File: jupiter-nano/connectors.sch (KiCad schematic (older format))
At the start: 0 parts

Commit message: WIP, connectors almost done
- still to do:
  - JTAG signals on PIO pins
  - USB-UART bridge
  - extra PIO on the header pins
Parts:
- added C28: 10uF, symbol Device:C
- added J5: Micro_SD_Card_Det_Hirose_DM3AT, symbol Connector:Micro_SD_Card_Det_Hirose_DM3AT
- added J5, J7, J8: USB_B_Micro, symbol Connector:USB_B_Micro
- added J6: Conn_01x02, symbol Connector_Generic:Conn_01x02
- added J9: Conn_ARM_JTAG_SWD_10, symbol Connector:Conn_ARM_JTAG_SWD_10
- added M3, MH4: MountingHole, symbol Mechanical:MountingHole
- added MH1, MH2: Conn_01x01, symbol Connector_Generic:Conn_01x01
- added R30: 10K, symbol Device:R_Small
- added R31: 68k, symbol Device:R_Small
- added R32, R33, R34: 68K, symbol Device:R_Small
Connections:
- new net CGND: J5.11 (SHIELD), J5.6 (Shield), J7.6 (Shield), J8.6 (Shield), MH1.1 (Pin_1), MH2.1 (Pin_1)
- new net GND: C28.1, J5.5 (GND), J5.6 (VSS), J7.5 (GND), J8.5 (GND), J9.3 (GND), J9.5 (GND), J9.9 (GNDDetect)
- new net HSIC_DATA: J6.2 (Pin_2)
- new net HSIC_STROBE: J6.1 (Pin_1)
- new net JTAG_TCK_PD14: J9.4 (SWDCLK/TCK)
- new net JTAG_TDI_PD15: J9.8 (NC/TDI)
- new net JTAG_TDO_PD16: J9.6 (SWO/TDO)
- new net JTAG_TMS_PD17: J9.2 (SWDIO/TMS)
- new net NRST: J9.10 (~RESET~)
- new net SDMMC1_CK: J5.5 (CLK)
- new net SDMMC1_CMD: J5.3 (CMD), R30.1
- new net SDMMC1_DAT0: J5.7 (DAT0), R33.1
- new net SDMMC1_DAT1: J5.8 (DAT1), R34.1
- new net SDMMC1_DAT2: J5.1 (DAT2), R31.1
- new net SDMMC1_DAT3: J5.2 (DAT3/CD), R32.1
- new net USBA_M: J5.2 (D-)
- new net USBA_P: J5.3 (D+)
- new net USBB_M: J7.2 (D-)
- new net USBB_P: J7.3 (D+)
- new net USBU_M: J8.2 (D-)
- new net USBU_P: J8.3 (D+)
- new net VBUS: J5.1 (VBUS), J7.1 (VBUS), J8.1 (VBUS)
- new net VDD_3V3: C28.2, J5.4 (VDD), J9.1 (VTref), R30.2, R31.2, R32.2, R33.2, R34.2
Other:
- note added: "JTAG"
- note added: "MicroSD"
- note added: "Mounting Holes"
- note added: "TODO: JTAG"
- note added: "TODO: card detect"
- note added: "USB"
- note added: "USB-UART Bridge"

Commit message: WIP, USB-UART and JTAG done
- minor clean up and SD Card form factor still left
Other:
- note removed: "TODO: JTAG"
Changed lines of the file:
@@
 Text Notes 6750 2650 0    79   ~ 0
 TODO: card detect
-Text Notes 3700 2200 0    79   ~ 0
-TODO: JTAG
 $Comp
 L starcat:CGND #PWR?

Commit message: cleanup
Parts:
- added R120: 10K, symbol Device:R_Small
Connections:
- net GND: now also R120.1
- net VDD_3V3: now also J5.10 (DET_A)
- net SDMMC1_CARD_DET: now reaches J5.9 (DET_B)
- net SDMMC1_CARD_DET: now also R120.2
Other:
- note added: "Native HSIC"
- note added: "Native USB Device"
- note added: "Native USB Host"
- note removed: "TODO: card detect"
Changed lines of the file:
@@
 Wire Wire Line
 	8500 2450 9550 2450
-Text Notes 6750 2650 0    79   ~ 0
-TODO: card detect
 $Comp
 L starcat:CGND #PWR?
@@
 Wire Wire Line
 	3100 2300 3100 2350
+Text Notes 1150 3850 0    79   ~ 0
+Native USB Host
+Text Notes 4200 3850 0    79   ~ 0
+Native USB Device
+Text Notes 7000 3800 0    79   ~ 0
+Native HSIC
+Wire Wire Line
+	6650 2650 6900 2650
+Wire Wire Line
+	6900 2650 6900 2900
+$Comp
+L Device:R_Small R120
+U 1 1 601FABB8
+P 6900 3000
+F 0 "R120" H 6841 2954 50  0000 R CNN
+F 1 "10K" H 6841 3045 50  0000 R CNN
+F 2 "" H 6900 3000 50  0001 C CNN
+F 3 "~" H 6900 3000 50  0001 C CNN
+	1    6900 3000
+	-1   0    0    1
+$EndComp
+Wire Wire Line
+	6900 3100 6900 3200
+$Comp
+L power:GND #PWR?
+U 1 1 602008BF
+P 6900 3200
+F 0 "#PWR?" H 6900 2950 50  0001 C CNN
+F 1 "GND" H 6905 3027 50  0000 C CNN
+F 2 "" H 6900 3200 50  0001 C CNN
+F 3 "" H 6900 3200 50  0001 C CNN
+	1    6900 3200
+	1    0    0    -1
+$EndComp
+Wire Wire Line
+	6900 2650 9550 2650
+Connection ~ 6900 2650
+Text GLabel 9550 2650 2    50   Input ~ 0
+SDMMC1_CARD_DET
+Wire Wire Line
+	6650 2550 9550 2550
+Text GLabel 9550 2550 2    50   Input ~ 0
+VDD_3V3
 $EndSCHEMATC

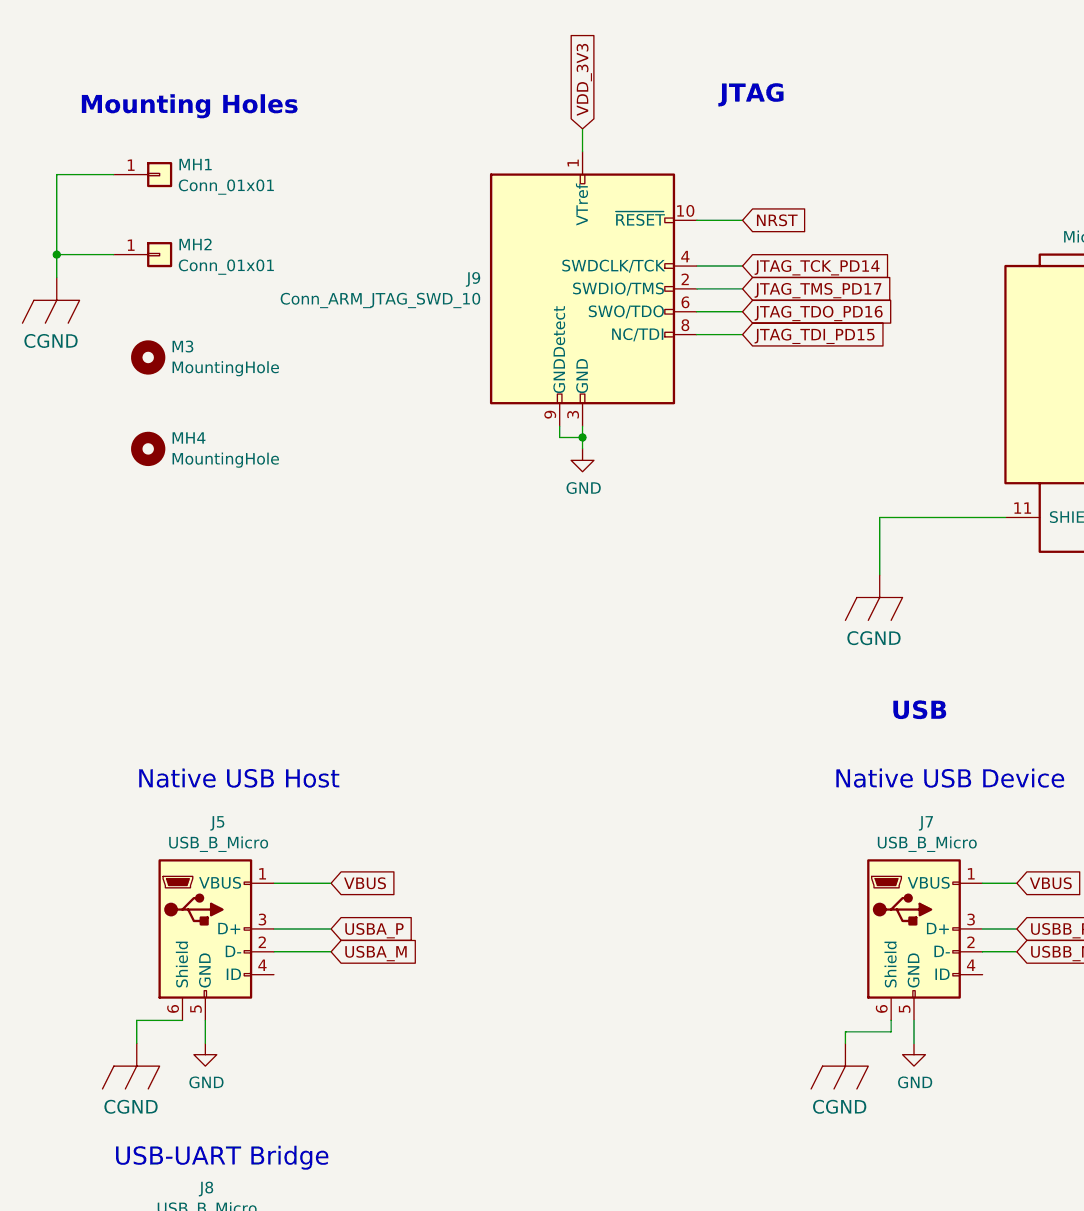
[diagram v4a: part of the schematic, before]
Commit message: add USBA VBUS sense; remove mounting holes
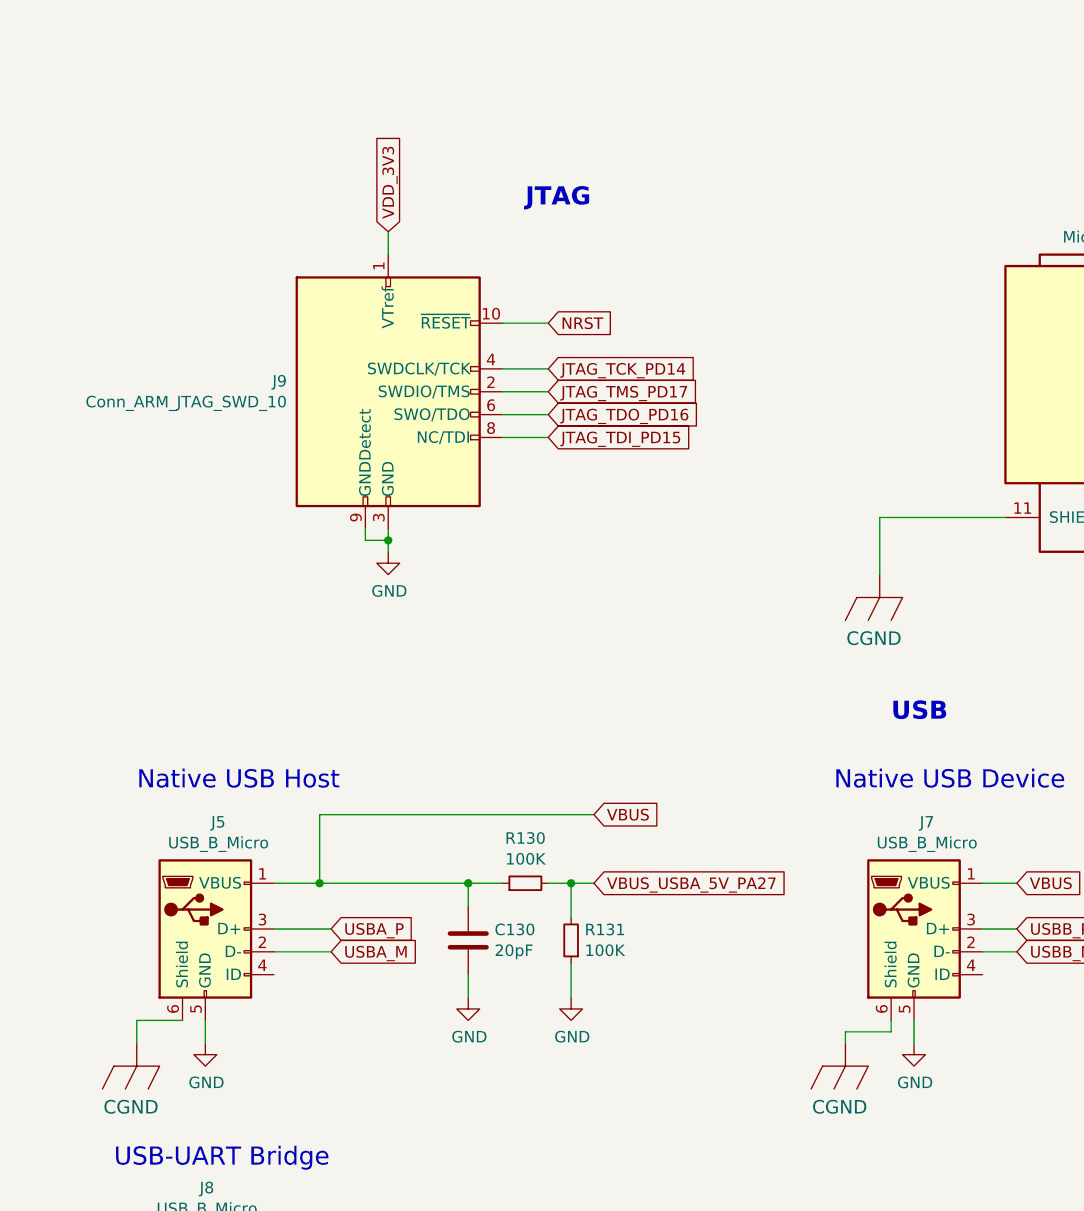
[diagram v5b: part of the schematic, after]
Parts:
- removed M3, MH4: MountingHole, symbol Mechanical:MountingHole
- removed MH1, MH2: Conn_01x01, symbol Connector_Generic:Conn_01x01
- added C130: 20pF, symbol Device:C
- added R130, R131: 100K, symbol Device:R_Small
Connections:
- net GND: now also C130.2, R131.1
- net VBUS: now also C130.1, R130.1
- new net VBUS_USBA_5V_PA27: R130.2, R131.2
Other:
- note removed: "Mounting Holes"
- moved on the sheet: J9
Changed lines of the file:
@@
 Comment4 ""
 $EndDescr
-Text Notes 900  900  0    79   ~ 16
-Mounting Holes
-$Comp
-L Connector_Generic:Conn_01x01 MH1
-U 1 1 600DDBE3
-P 1250 1150
-F 0 "MH1" H 1330 1192 50  0000 L CNN
-F 1 "Conn_01x01" H 1330 1101 50  0000 L CNN
-F 2 "" H 1250 1150 50  0001 C CNN
-F 3 "~" H 1250 1150 50  0001 C CNN
-	1    1250 1150
-	1    0    0    -1
-$EndComp
-$Comp
-L Connector_Generic:Conn_01x01 MH2
-U 1 1 600DE109
-P 1250 1500
-F 0 "MH2" H 1330 1542 50  0000 L CNN
-F 1 "Conn_01x01" H 1330 1451 50  0000 L CNN
-F 2 "" H 1250 1500 50  0001 C CNN
-F 3 "~" H 1250 1500 50  0001 C CNN
-	1    1250 1500
-	1    0    0    -1
-$EndComp
-$Comp
-L Mechanical:MountingHole M3
-U 1 1 600DE96A
-P 1200 1950
-F 0 "M3" H 1300 1996 50  0000 L CNN
-F 1 "MountingHole" H 1300 1905 50  0000 L CNN
-F 2 "" H 1200 1950 50  0001 C CNN
-F 3 "~" H 1200 1950 50  0001 C CNN
-	1    1200 1950
-	1    0    0    -1
-$EndComp
-$Comp
-L Mechanical:MountingHole MH4
-U 1 1 600DEB93
-P 1200 2350
-F 0 "MH4" H 1300 2396 50  0000 L CNN
-F 1 "MountingHole" H 1300 2305 50  0000 L CNN
-F 2 "" H 1200 2350 50  0001 C CNN
-F 3 "~" H 1200 2350 50  0001 C CNN
-	1    1200 2350
-	1    0    0    -1
-$EndComp
-Wire Wire Line
-	1050 1150 800  1150
-Wire Wire Line
-	800  1150 800  1500
-Wire Wire Line
-	800  1500 1050 1500
-Wire Wire Line
-	800  1500 800  1600
-Connection ~ 800  1500
-Text Notes 3700 850  0    79   ~ 16
+Text Notes 2850 1300 0    79   ~ 16
 JTAG
 Text Notes 7450 800  0    79   ~ 16
@@
 	1750 4550 2000 4550
 Wire Wire Line
-	1750 4250 2000 4250
-Wire Wire Line
 	1450 4850 1450 4950
 Wire Wire Line
@@
 Wire Wire Line
 	1400 6450 1400 6500
-Text GLabel 2000 4250 2    50   Input ~ 0
-VBUS
+Text GLabel 3150 4250 2    50   Input ~ 0
+VBUS_USBA_5V_PA27
 Text GLabel 5000 4250 2    50   Input ~ 0
 VBUS
@@
 Wire Wire Line
 	8500 2450 9550 2450
-$Comp
-L starcat:CGND #PWR?
-U 1 1 6019D543
-P 800 1700
-F 0 "#PWR?" H 800 1800 79  0001 C CNN
-F 1 "CGND" H 775 1520 59  0000 C CNN
-F 2 "" H 800 1800 79  0001 C CNN
-F 3 "" H 800 1800 79  0001 C CNN
-	1    800  1700
-	1    0    0    -1
-$EndComp
-Wire Wire Line
-	3600 1350 3800 1350
-Wire Wire Line
-	3600 1550 3800 1550
-Wire Wire Line
-	3600 1650 3800 1650
-Wire Wire Line
-	3600 1750 3800 1750
-Wire Wire Line
-	3600 1850 3800 1850
-Wire Wire Line
-	3100 2250 3100 2300
+Wire Wire Line
+	2750 1800 2950 1800
+Wire Wire Line
+	2750 2000 2950 2000
+Wire Wire Line
+	2750 2100 2950 2100
+Wire Wire Line
+	2750 2200 2950 2200
+Wire Wire Line
+	2750 2300 2950 2300
+Wire Wire Line
+	2250 2700 2250 2750
 $Comp
 L power:GND #PWR?
 U 1 1 601B02C7
-P 3100 2350
-F 0 "#PWR?" H 3100 2100 50  0001 C CNN
-F 1 "GND" H 3105 2177 50  0000 C CNN
-F 2 "" H 3100 2350 50  0001 C CNN
-F 3 "" H 3100 2350 50  0001 C CNN
-	1    3100 2350
-	1    0    0    -1
-$EndComp
-Text GLabel 3800 1350 2    50   Input ~ 0
+P 2250 2800
+F 0 "#PWR?" H 2250 2550 50  0001 C CNN
+F 1 "GND" H 2255 2627 50  0000 C CNN
+F 2 "" H 2250 2800 50  0001 C CNN
+F 3 "" H 2250 2800 50  0001 C CNN
+	1    2250 2800
+	1    0    0    -1
+$EndComp
+Text GLabel 2950 1800 2    50   Input ~ 0
 NRST
-Text GLabel 3800 1550 2    50   Input ~ 0
+Text GLabel 2950 2000 2    50   Input ~ 0
 JTAG_TCK_PD14
-Text GLabel 3800 1650 2    50   Input ~ 0
+Text GLabel 2950 2100 2    50   Input ~ 0
 JTAG_TMS_PD17
-Text GLabel 3800 1750 2    50   Input ~ 0
+Text GLabel 2950 2200 2    50   Input ~ 0
 JTAG_TDO_PD16
-Text GLabel 3800 1850 2    50   Input ~ 0
+Text GLabel 2950 2300 2    50   Input ~ 0
 JTAG_TDI_PD15
 $Comp
 L Connector:Conn_ARM_JTAG_SWD_10 J9
 U 1 1 601B413A
-P 3100 1650
-F 0 "J9" H 2657 1696 50  0000 R CNN
-F 1 "Conn_ARM_JTAG_SWD_10" H 2657 1605 50  0000 R CNN
-F 2 "" H 3100 1650 50  0001 C CNN
-F 3 "http://infocenter.arm.com/help/topic/com.arm.doc.ddi0314h/DDI0314H_coresight_components_trm.pdf" V 2750 400 50  0001 C CNN
-	1    3100 1650
-	1    0    0    -1
-$EndComp
-Text GLabel 3100 950  1    50   Input ~ 0
+P 2250 2100
+F 0 "J9" H 1807 2146 50  0000 R CNN
+F 1 "Conn_ARM_JTAG_SWD_10" H 1807 2055 50  0000 R CNN
+F 2 "" H 2250 2100 50  0001 C CNN
+F 3 "http://infocenter.arm.com/help/topic/com.arm.doc.ddi0314h/DDI0314H_coresight_components_trm.pdf" V 1900 850 50  0001 C CNN
+	1    2250 2100
+	1    0    0    -1
+$EndComp
+Text GLabel 2250 1400 1    50   Input ~ 0
 VDD_3V3
 Wire Wire Line
-	3100 1050 3100 950
-Wire Wire Line
-	3000 2250 3000 2300
-Wire Wire Line
-	3000 2300 3100 2300
-Connection ~ 3100 2300
-Wire Wire Line
-	3100 2300 3100 2350
+	2250 1500 2250 1400
+Wire Wire Line
+	2150 2700 2150 2750
+Wire Wire Line
+	2150 2750 2250 2750
+Connection ~ 2250 2750
+Wire Wire Line
+	2250 2750 2250 2800
 Text Notes 1150 3850 0    79   ~ 0
 Native USB Host
@@
 Text GLabel 9550 2550 2    50   Input ~ 0
 VDD_3V3
+Text GLabel 3150 3950 2    50   Input ~ 0
+VBUS
+$Comp
+L Device:R_Small R131
+U 1 1 60356F20
+P 3050 4500
+F 0 "R131" H 2991 4454 50  0000 R CNN
+F 1 "100K" H 2991 4545 50  0000 R CNN
+F 2 "" H 3050 4500 50  0001 C CNN
+F 3 "~" H 3050 4500 50  0001 C CNN
+	1    3050 4500
+	-1   0    0    1
+$EndComp
+$Comp
+L Device:R_Small R130
+U 1 1 60357730
+P 2850 4250
+F 0 "R130" V 3046 4250 50  0000 C CNN
+F 1 "100K" V 2955 4250 50  0000 C CNN
+F 2 "" H 2850 4250 50  0001 C CNN
+F 3 "~" H 2850 4250 50  0001 C CNN
+	1    2850 4250
+	0    -1   -1   0
+$EndComp
+$Comp
+L Device:C C130
+U 1 1 60357A00
+P 2600 4500
+F 0 "C130" H 2715 4546 50  0000 L CNN
+F 1 "20pF" H 2715 4455 50  0000 L CNN
+F 2 "" H 2638 4350 50  0001 C CNN
+F 3 "~" H 2600 4500 50  0001 C CNN
+	1    2600 4500
+	1    0    0    -1
+$EndComp
+Wire Wire Line
+	1750 4250 1950 4250
+Wire Wire Line
+	2600 4350 2600 4250
+Connection ~ 2600 4250
+Wire Wire Line
+	2600 4250 2750 4250
+Wire Wire Line
+	2950 4250 3050 4250
+Wire Wire Line
+	3050 4400 3050 4250
+Connection ~ 3050 4250
+Wire Wire Line
+	3050 4250 3150 4250
+Wire Wire Line
+	2600 4650 2600 4750
+$Comp
+L power:GND #PWR?
+U 1 1 60363D58
+P 2600 4750
+F 0 "#PWR?" H 2600 4500 50  0001 C CNN
+F 1 "GND" H 2605 4577 50  0000 C CNN
+F 2 "" H 2600 4750 50  0001 C CNN
+F 3 "" H 2600 4750 50  0001 C CNN
+	1    2600 4750
+	1    0    0    -1
+$EndComp
+Wire Wire Line
+	3050 4600 3050 4750
+$Comp
+L power:GND #PWR?
+U 1 1 60366200
+P 3050 4750
+F 0 "#PWR?" H 3050 4500 50  0001 C CNN
+F 1 "GND" H 3055 4577 50  0000 C CNN
+F 2 "" H 3050 4750 50  0001 C CNN
+F 3 "" H 3050 4750 50  0001 C CNN
+	1    3050 4750
+	1    0    0    -1
+$EndComp
+Wire Wire Line
+	3150 3950 1950 3950
+Wire Wire Line
+	1950 3950 1950 4250
+Connection ~ 1950 4250
+Wire Wire Line
+	1950 4250 2600 4250
 $EndSCHEMATC

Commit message: numerous ERC fixes
- still more to go
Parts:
- added D301: RED LED, symbol Device:LED
- added D302: BLUE LED, symbol Device:LED
- added R301, R302: 330R, symbol Device:R_Small
- added R350: 0R, symbol Device:R_Small
- renumbered C130 to C6, C28 to C7, J8 to J1, J5 to J2, J9 to J3, J7 to J4, R32 to R10, R33 to R11, R34 to R12, R130 to R5, R131 to R6, R30 to R7, R120 to R8, R31 to R9
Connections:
- net CGND: no longer J5.11 (SHIELD)
- net GND: now also J5.11 (SHIELD), R301.2, R302.2, R350.2
- net VDD_3V3: now also D301.2 (A)
- net VBUS renamed +5V
- new net: D302.1 (K), R302.1
- new net: D301.1 (K), R301.1
- new net SDMMC1_CD: R350.1
- new net STATUS_LED: D302.2 (A)
- no-connect marks 0 -> 3
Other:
- note added: "LEDs"
